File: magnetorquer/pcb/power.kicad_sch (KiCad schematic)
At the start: 3 parts, among them J7 Conn_01x02_Pin

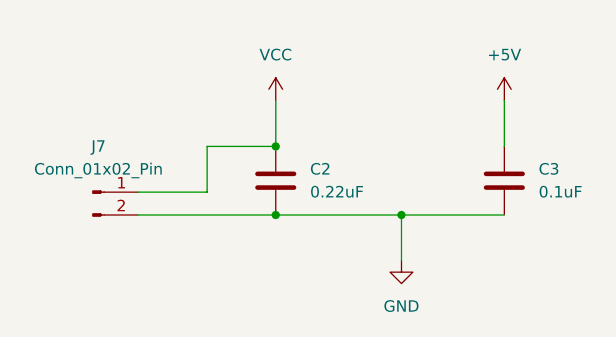
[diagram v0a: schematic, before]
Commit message: Power reg. and v.1 print
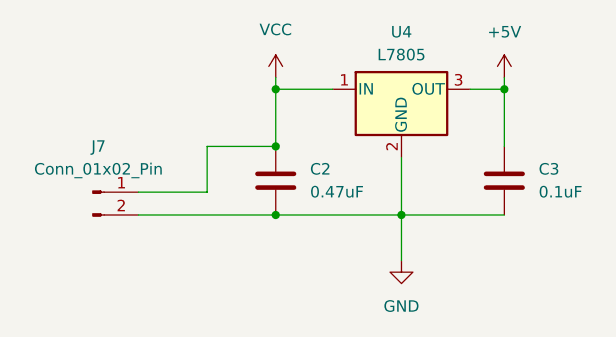
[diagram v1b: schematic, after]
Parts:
- added U4: L7805, Package_TO_SOT_THT:TO-220-3_Horizontal_TabDown, symbol Regulator_Linear:L7805
- C2: value 0.22uF -> 0.47uF; footprint Capacitor_THT:C_Rect_L7.0mm_W2.5mm_P5.00mm -> Capacitor_THT:C_Rect_L7.0mm_W4.5mm_P5.00mm
- C3: footprint Capacitor_THT:C_Rect_L7.0mm_W2.5mm_P5.00mm -> Capacitor_THT:C_Rect_L7.0mm_W2.0mm_P5.00mm
- J7: footprint Connector_PinHeader_2.54mm:PinHeader_1x02_P2.54mm_Vertical -> TerminalBlock:TerminalBlock_MaiXu_MX126-5.0-02P_1x02_P5.00mm
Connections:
- net +5V: now also U4.3 (OUT)
- net GND: now also U4.2 (GND)
- net VCC: now also U4.1 (IN)
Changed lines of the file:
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@@
 	(paper "A4")
+	(junction
+		(at 104.14 67.31)
+		(diameter 0)
+		(color 0 0 0 0)
+	)
 	(junction
 		(at 78.74 73.66)
@@
 	)
 	(junction
+		(at 78.74 67.31)
+		(diameter 0)
+		(color 0 0 0 0)
+	)
+	(junction
 		(at 78.74 81.28)
 		(diameter 0)
@@
 	(wire
 		(pts
-			(xy 104.14 68.58) (xy 104.14 73.66)
+			(xy 104.14 66.04) (xy 104.14 67.31)
+		)
+		(stroke
+			(width 0)
+			(type default)
+		)
+	)
+	(wire
+		(pts
+			(xy 92.71 74.93) (xy 92.71 81.28)
 		)
 		(stroke
@@
 	(wire
 		(pts
+			(xy 78.74 67.31) (xy 78.74 73.66)
+		)
+		(stroke
+			(width 0)
+			(type default)
+		)
+	)
+	(wire
+		(pts
 			(xy 63.5 78.74) (xy 71.12 78.74)
 		)
@@
 	(wire
 		(pts
-			(xy 78.74 68.58) (xy 78.74 73.66)
+			(xy 100.33 67.31) (xy 104.14 67.31)
+		)
+		(stroke
+			(width 0)
+			(type default)
+		)
+	)
+	(wire
+		(pts
+			(xy 78.74 66.04) (xy 78.74 67.31)
 		)
 		(stroke
@@
 		)
 	)
+	(wire
+		(pts
+			(xy 104.14 67.31) (xy 104.14 73.66)
+		)
+		(stroke
+			(width 0)
+			(type default)
+		)
+	)
+	(wire
+		(pts
+			(xy 78.74 67.31) (xy 85.09 67.31)
+		)
+		(stroke
+			(width 0)
+			(type default)
+		)
+	)
 	(symbol
 		(lib_id "power:+5V")
-		(at 104.14 68.58 0)
+		(at 104.14 66.04 0)
 		(unit 1)
 		(exclude_from_sim no)
@@
 		(fields_autoplaced yes)
 		(property "Reference" "#PWR010"
-			(at 104.14 72.39 0)
+			(at 104.14 69.85 0)
 			(effects
 				(font
@@
 		)
 		(property "Value" "+5V"
-			(at 104.14 63.5 0)
+			(at 104.14 60.96 0)
 			(effects
 				(font
@@
 		)
 		(property "Footprint" ""
-			(at 104.14 68.58 0)
+			(at 104.14 66.04 0)
 			(effects
 				(font
@@
 		)
 		(property "Datasheet" ""
-			(at 104.14 68.58 0)
+			(at 104.14 66.04 0)
 			(effects
 				(font
@@
 		)
 		(property "Description" "Power symbol creates a global label with name \"+5V\""
-			(at 104.14 68.58 0)
+			(at 104.14 66.04 0)
 			(effects
 				(font
@@
 			)
 		)
-		(property "Value" "0.22uF"
+		(property "Value" "0.47uF"
 			(at 82.55 78.7399 0)
 			(effects
@@
 			)
 		)
-		(property "Footprint" "Capacitor_THT:C_Rect_L7.0mm_W2.5mm_P5.00mm"
+		(property "Footprint" "Capacitor_THT:C_Rect_L7.0mm_W4.5mm_P5.00mm"
 			(at 79.7052 81.28 0)
 			(effects
@@
 			)
 		)
-		(property "Footprint" "Capacitor_THT:C_Rect_L7.0mm_W2.5mm_P5.00mm"
+		(property "Footprint" "Capacitor_THT:C_Rect_L7.0mm_W2.0mm_P5.00mm"
 			(at 105.1052 81.28 0)
 			(effects
@@
 			)
 		)
-		(property "Footprint" "Connector_PinHeader_2.54mm:PinHeader_1x02_P2.54mm_Vertical"
+		(property "Footprint" "TerminalBlock:TerminalBlock_MaiXu_MX126-5.0-02P_1x02_P5.00mm"
 			(at 58.42 78.74 0)
 			(effects
@@
 	)
 	(symbol
+		(lib_id "Regulator_Linear:L7805")
+		(at 92.71 67.31 0)
+		(unit 1)
+		(exclude_from_sim no)
+		(in_bom yes)
+		(on_board yes)
+		(dnp no)
+		(fields_autoplaced yes)
+		(property "Reference" "U4"
+			(at 92.71 60.96 0)
+			(effects
+				(font
+					(size 1.27 1.27)
+				)
+			)
+		)
+		(property "Value" "L7805"
+			(at 92.71 63.5 0)
+			(effects
+				(font
+					(size 1.27 1.27)
+				)
+			)
+		)
+		(property "Footprint" "Package_TO_SOT_THT:TO-220-3_Horizontal_TabDown"
+			(at 93.345 71.12 0)
+			(effects
+				(font
+					(size 1.27 1.27)
+					(italic yes)
+				)
+				(justify left)
+				(hide yes)
+			)
+		)
+		(property "Datasheet" "http://www.st.com/content/ccc/resource/technical/document/datasheet/41/4f/b3/b0/12/d4/47/88/CD00000444.pdf/files/CD00000444.pdf/jcr:content/translations/en.CD00000444.pdf"
+			(at 92.71 68.58 0)
+			(effects
+				(font
+					(size 1.27 1.27)
+				)
+				(hide yes)
+			)
+		)
+		(property "Description" "Positive 1.5A 35V Linear Regulator, Fixed Output 5V, TO-220/TO-263/TO-252"
+			(at 92.71 67.31 0)
+			(effects
+				(font
+					(size 1.27 1.27)
+				)
+				(hide yes)
+			)
+		)
+		(pin "3"
+		)
+		(pin "2"
+		)
+		(pin "1"
+		)
+		(instances
+			(project ""
+				(path "/14c04de7-71ee-4f20-9e6e-041dbb035733/eb4b2821-746d-4b25-ad4a-ccbed5b39359"
+					(reference "U4")
+					(unit 1)
+				)
+			)
+		)
+	)
+	(symbol
 		(lib_id "power:VCC")
-		(at 78.74 68.58 0)
-		(unit 1)
-		(exclude_from_sim no)
-		(in_bom yes)
-		(on_board yes)
-		(dnp no)
-		(fields_autoplaced yes)
+		(at 78.74 66.04 0)
+		(unit 1)
+		(exclude_from_sim no)
+		(in_bom yes)
+		(on_board yes)
+		(dnp no)
 		(property "Reference" "#PWR08"
-			(at 78.74 72.39 0)
+			(at 78.74 69.85 0)
 			(effects
 				(font
@@
 		)
 		(property "Value" "VCC"
-			(at 78.74 63.5 0)
+			(at 78.74 60.706 0)
 			(effects
 				(font
@@
 		)
 		(property "Footprint" ""
-			(at 78.74 68.58 0)
+			(at 78.74 66.04 0)
 			(effects
 				(font
@@
 		)
 		(property "Datasheet" ""
-			(at 78.74 68.58 0)
+			(at 78.74 66.04 0)
 			(effects
 				(font
@@
 		)
 		(property "Description" "Power symbol creates a global label with name \"VCC\""
-			(at 78.74 68.58 0)
-			(effects
-				(font
+			(at 78.74 66.04 0)
+			(effects
+				(font
